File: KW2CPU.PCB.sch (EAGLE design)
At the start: 66 parts, among them J1 DF12_M, J2 MOLEX55560-0207, J3 MMCX_VERT, U1 MKW21D, U2 AT45DB161D8S1, U3 RF6555, U5 F-ANTENNA, X1 32KHZ, X2 32MHZ

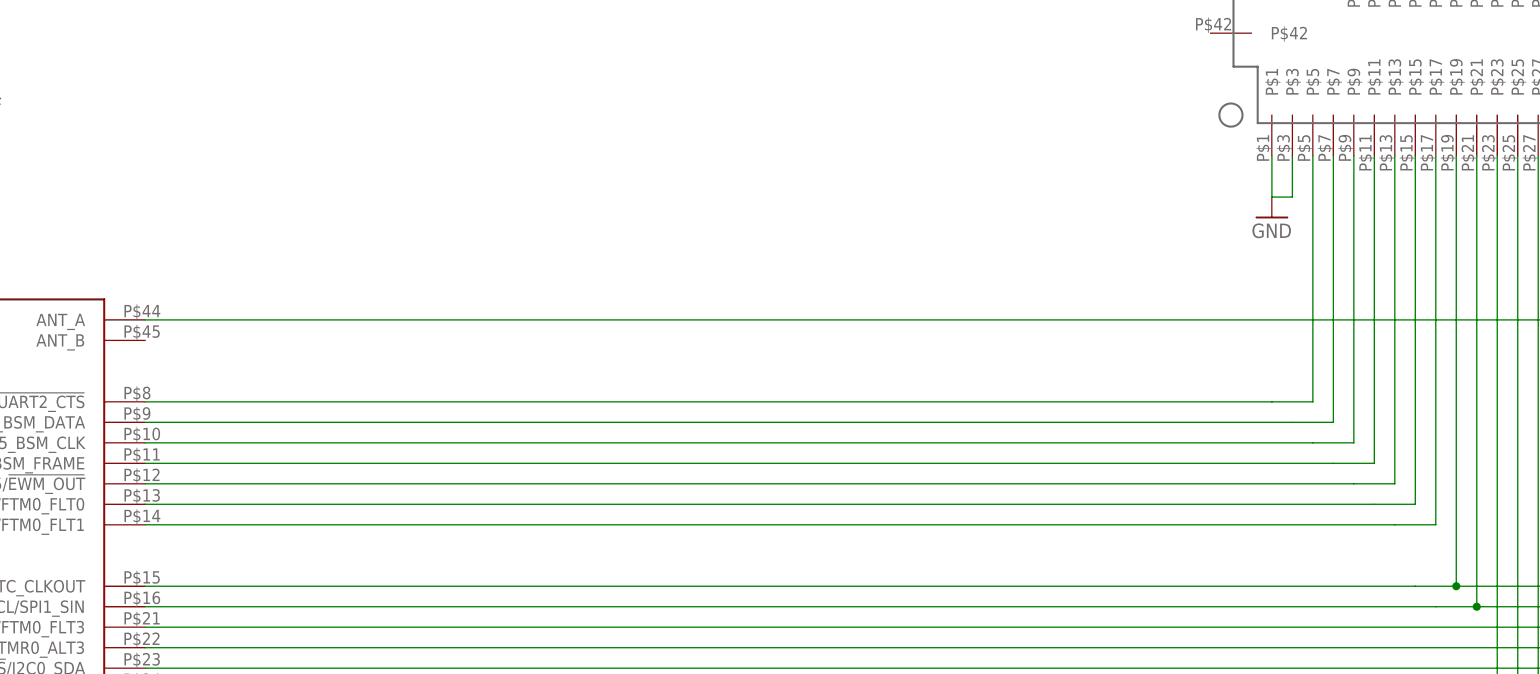
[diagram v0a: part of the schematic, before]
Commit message: Added timing TPs
For radio calibration. Also exported CAD model
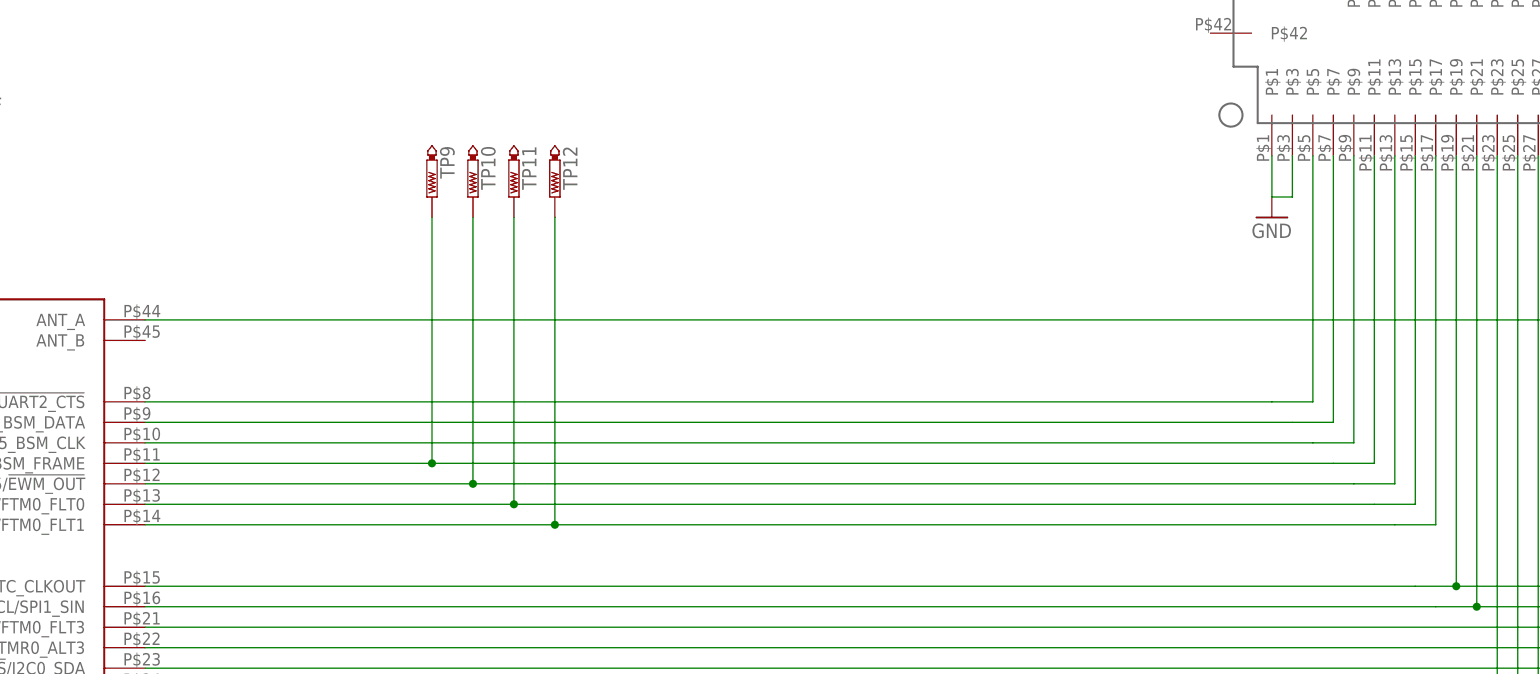
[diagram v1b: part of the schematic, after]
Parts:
- added TP10, TP11, TP12, TP9: PTR1TP15R, testpad:PTR1TP15R
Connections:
- net PTD4/LLWU_P14/MADC0_SE21/SPI0_PCS1/!UART0_RTS!/FTM0_CH4/EWM_IN/GPIO_BSM_FRAME: now also TP9.TP
- net PTD5/ADC0_SE6B/SPI0_PCS2/!UART0_CTS!/!UART0_COL!/FTM0_CH5/!EWM_OUT: now also TP10.TP
- net PTD6/LLWU_P15/ADC0_SE7B/SPI0_PCS3/UART0_RX/FTM0_CH6/FTM0_FLT0: now also TP11.TP
- net PTD7/MADC0_SE22/CMT_IRO/UART0_TX/FTM0_CH7/FTM0_FLT1: now also TP12.TP
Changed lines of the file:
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@@
 <part name="TP7" library="testpad" deviceset="PTR1" device="TP15R"/>
 <part name="TP8" library="testpad" deviceset="PTR1" device="TP15R"/>
+<part name="TP9" library="testpad" deviceset="PTR1" device="TP15R"/>
+<part name="TP10" library="testpad" deviceset="PTR1" device="TP15R"/>
+<part name="TP11" library="testpad" deviceset="PTR1" device="TP15R"/>
+<part name="TP12" library="testpad" deviceset="PTR1" device="TP15R"/>
 </parts>
 <sheets>
@@
 <instance part="TP7" gate="G$1" x="292.1" y="106.68" rot="R180"/>
 <instance part="TP8" gate="G$1" x="350.52" y="53.34" rot="R180"/>
+<instance part="TP9" gate="G$1" x="101.6" y="63.5" rot="R180"/>
+<instance part="TP10" gate="G$1" x="106.68" y="63.5" rot="R180"/>
+<instance part="TP11" gate="G$1" x="111.76" y="63.5" rot="R180"/>
+<instance part="TP12" gate="G$1" x="116.84" y="63.5" rot="R180"/>
 </instances>
 <busses>
@@
 <segment>
 <pinref part="U1" gate="G$1" pin="PTD4/LLWU_P14/MADC0_SE21/SPI0_PCS1/!UART0_RTS!/FTM0_CH4/EWM_IN/GPIO_BSM_FRAME"/>
-<wire x1="66.04" y1="30.48" x2="213.36" y2="30.48" width="0.1524" layer="91"/>
+<wire x1="66.04" y1="30.48" x2="101.6" y2="30.48" width="0.1524" layer="91"/>
 <pinref part="J1" gate="G$1" pin="P$11"/>
+<wire x1="101.6" y1="30.48" x2="213.36" y2="30.48" width="0.1524" layer="91"/>
 <wire x1="213.36" y1="30.48" x2="218.44" y2="30.48" width="0.1524" layer="91"/>
 <wire x1="218.44" y1="30.48" x2="218.44" y2="68.58" width="0.1524" layer="91"/>
+<pinref part="TP9" gate="G$1" pin="TP"/>
+<wire x1="101.6" y1="60.96" x2="101.6" y2="30.48" width="0.1524" layer="91"/>
+<junction x="101.6" y="30.48"/>
 </segment>
 </net>
@@
 <segment>
 <pinref part="U1" gate="G$1" pin="PTD5/ADC0_SE6B/SPI0_PCS2/!UART0_CTS!/!UART0_COL!/FTM0_CH5/!EWM_OUT"/>
-<wire x1="66.04" y1="27.94" x2="215.9" y2="27.94" width="0.1524" layer="91"/>
+<wire x1="66.04" y1="27.94" x2="106.68" y2="27.94" width="0.1524" layer="91"/>
 <pinref part="J1" gate="G$1" pin="P$13"/>
+<wire x1="106.68" y1="27.94" x2="215.9" y2="27.94" width="0.1524" layer="91"/>
 <wire x1="215.9" y1="27.94" x2="220.98" y2="27.94" width="0.1524" layer="91"/>
 <wire x1="220.98" y1="27.94" x2="220.98" y2="68.58" width="0.1524" layer="91"/>
+<pinref part="TP10" gate="G$1" pin="TP"/>
+<wire x1="106.68" y1="60.96" x2="106.68" y2="27.94" width="0.1524" layer="91"/>
+<junction x="106.68" y="27.94"/>
 </segment>
 </net>
@@
 <segment>
 <pinref part="U1" gate="G$1" pin="PTD6/LLWU_P15/ADC0_SE7B/SPI0_PCS3/UART0_RX/FTM0_CH6/FTM0_FLT0"/>
-<wire x1="66.04" y1="25.4" x2="218.44" y2="25.4" width="0.1524" layer="91"/>
+<wire x1="66.04" y1="25.4" x2="111.76" y2="25.4" width="0.1524" layer="91"/>
 <pinref part="J1" gate="G$1" pin="P$15"/>
+<wire x1="111.76" y1="25.4" x2="218.44" y2="25.4" width="0.1524" layer="91"/>
 <wire x1="218.44" y1="25.4" x2="223.52" y2="25.4" width="0.1524" layer="91"/>
 <wire x1="223.52" y1="25.4" x2="223.52" y2="68.58" width="0.1524" layer="91"/>
+<pinref part="TP11" gate="G$1" pin="TP"/>
+<wire x1="111.76" y1="60.96" x2="111.76" y2="25.4" width="0.1524" layer="91"/>
+<junction x="111.76" y="25.4"/>
 </segment>
 </net>
@@
 <segment>
 <pinref part="U1" gate="G$1" pin="PTD7/MADC0_SE22/CMT_IRO/UART0_TX/FTM0_CH7/FTM0_FLT1"/>
-<wire x1="66.04" y1="22.86" x2="220.98" y2="22.86" width="0.1524" layer="91"/>
+<wire x1="66.04" y1="22.86" x2="116.84" y2="22.86" width="0.1524" layer="91"/>
 <pinref part="J1" gate="G$1" pin="P$17"/>
+<wire x1="116.84" y1="22.86" x2="220.98" y2="22.86" width="0.1524" layer="91"/>
 <wire x1="220.98" y1="22.86" x2="226.06" y2="22.86" width="0.1524" layer="91"/>
 <wire x1="226.06" y1="22.86" x2="226.06" y2="68.58" width="0.1524" layer="91"/>
-</segment>
-</net>
+<pinref part="TP12" gate="G$1" pin="TP"/>
+<wire x1="116.84" y1="60.96" x2="116.84" y2="22.86" width="0.1524" layer="91"/>
+<junction x="116.84" y="22.86"/>
+</segment>
+</net>

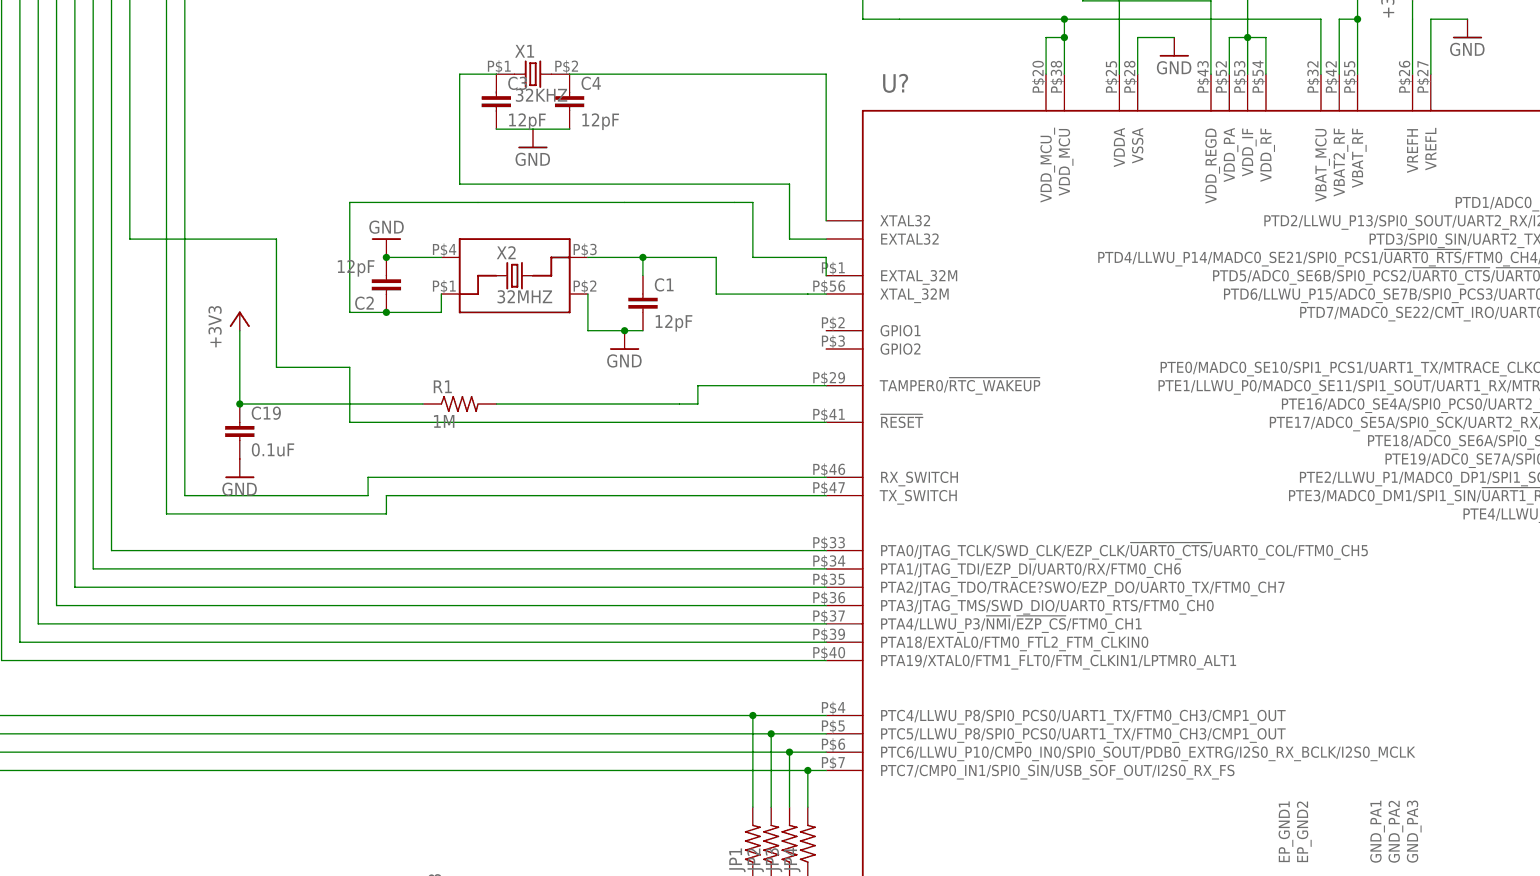
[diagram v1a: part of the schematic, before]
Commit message: Fixed PTC5 label and added RESET pullup
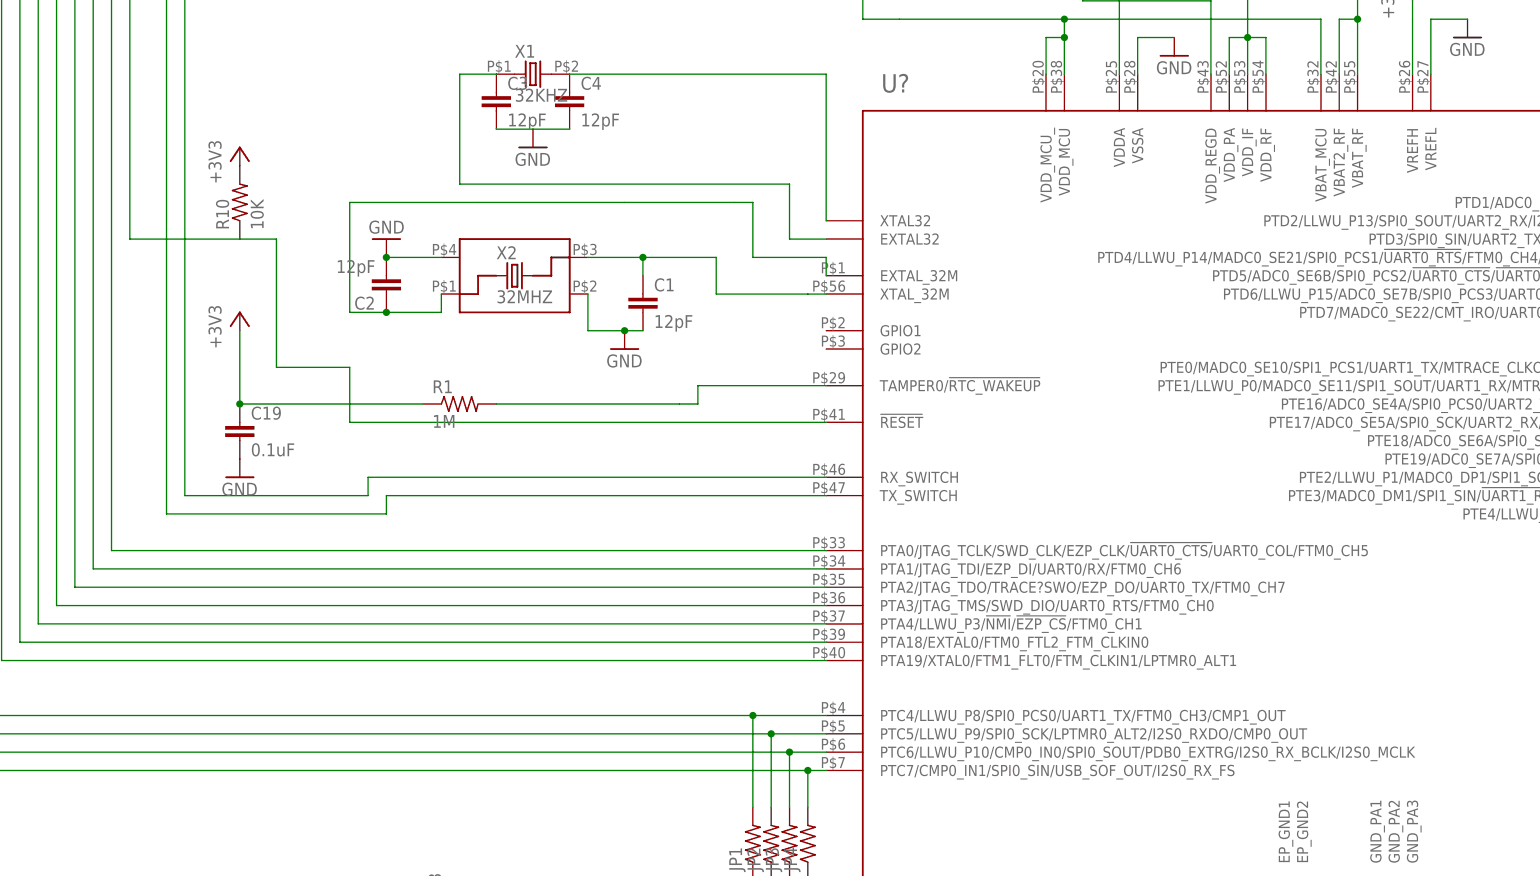
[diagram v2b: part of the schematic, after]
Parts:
- added R10: 10K, GW-devices:RF-R0402
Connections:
- net !RESET: now also R10.1
- net +3V3: now also R10.2
- net PTC5/LLWU_P8/SPI0_PCS0/UART1_TX/FTM0_CH3/CMP1_OUT: now also U1.PTC5/LLWU_P9/SPI0_SCK/LPTMR0_ALT2/I2S0_RXDO/CMP0_OUT; no longer U1.PTC5/LLWU_P8/SPI0_PCS0/UART1_TX/FTM0_CH3/CMP1_OUT
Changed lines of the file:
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@@
 <part name="TP11" library="testpad" deviceset="PTR1" device="TP15R"/>
 <part name="TP12" library="testpad" deviceset="PTR1" device="TP15R"/>
+<part name="R10" library="GW-devices" deviceset="RF-R" device="0402" value="10K"/>
+<part name="+3V14" library="supply1" deviceset="+3V3" device=""/>
 </parts>
 <sheets>
@@
 <instance part="TP11" gate="G$1" x="111.76" y="63.5" rot="R180"/>
 <instance part="TP12" gate="G$1" x="116.84" y="63.5" rot="R180"/>
+<instance part="R10" gate="G$1" x="-147.32" y="38.1" rot="R90"/>
+<instance part="+3V14" gate="G$1" x="-147.32" y="45.72"/>
 </instances>
 <busses>
@@
 <pinref part="J2" gate="G$1" pin="P$1"/>
 </segment>
+<segment>
+<pinref part="R10" gate="G$1" pin="2"/>
+<pinref part="+3V14" gate="G$1" pin="+3V3"/>
+</segment>
 </net>
 <net name="EXTAL_32M" class="0">
@@
 <net name="PTC5/LLWU_P8/SPI0_PCS0/UART1_TX/FTM0_CH3/CMP1_OUT" class="0">
 <segment>
-<pinref part="U1" gate="G$1" pin="PTC5/LLWU_P8/SPI0_PCS0/UART1_TX/FTM0_CH3/CMP1_OUT"/>
+<pinref part="U1" gate="G$1" pin="PTC5/LLWU_P9/SPI0_SCK/LPTMR0_ALT2/I2S0_RXDO/CMP0_OUT"/>
 <wire x1="-73.66" y1="-35.56" x2="-66.04" y2="-35.56" width="0.1524" layer="91"/>
 <pinref part="J1" gate="G$1" pin="P$24"/>
@@
 <wire x1="-132.08" y1="15.24" x2="-142.24" y2="15.24" width="0.1524" layer="91"/>
 <wire x1="-142.24" y1="15.24" x2="-142.24" y2="33.02" width="0.1524" layer="91"/>
-<wire x1="-142.24" y1="33.02" x2="-162.56" y2="33.02" width="0.1524" layer="91"/>
+<wire x1="-142.24" y1="33.02" x2="-147.32" y2="33.02" width="0.1524" layer="91"/>
+<wire x1="-147.32" y1="33.02" x2="-162.56" y2="33.02" width="0.1524" layer="91"/>
 <wire x1="-162.56" y1="33.02" x2="-162.56" y2="121.92" width="0.1524" layer="91"/>
 <wire x1="-162.56" y1="121.92" x2="205.74" y2="121.92" width="0.1524" layer="91"/>
@@
 <wire x1="297.18" y1="142.24" x2="297.18" y2="121.92" width="0.1524" layer="91"/>
 <junction x="297.18" y="121.92"/>
-</segment>
-</net>
+<pinref part="R10" gate="G$1" pin="1"/>
+</segment>
+</net>

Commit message: Switched Flash for EEPROM
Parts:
- removed JP1, JP2, JP3, JP4: (no value), GW-devices:RF-R0402
- removed R2, R3: 10k, GW-devices:RF-R0402
- removed U2: AT45DB161D8S1, KW2:AT45DB161D8S1
- added IC1: 25AA080SN, microchip:25AA080SN
- added R11, R12: 10k, GW-devices:RF-R0402
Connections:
- removed net !CS: JP1.1, U2.!CS
- removed net N$54: JP4.1, U2.SO
- removed net N$8: R3.1, U2.!RESET
- removed net N$9: R2.1, U2.!WP
- removed net SCK: JP2.1, U2.SCK
- removed net SI: JP3.1, U2.SI
- new net N$1: IC1.!WP, R11.1
- new net N$2: IC1.!HOLD, R12.1
- net +3V3: now also IC1.VCC, R11.2, R12.2; no longer R2.2, R3.2, U2.VCC
- net GND: now also IC1.GND; no longer U2.GND
- net PTC4/LLWU_P8/SPI0_PCS0/UART1_TX/FTM0_CH3/CMP1_OUT: no longer JP1.2
- net PTC5/LLWU_P8/SPI0_PCS0/UART1_TX/FTM0_CH3/CMP1_OUT: now also IC1.SCK; no longer JP2.2
- net PTC6/LLWU_P10/CMP0_IN0/SPI0_SOUT/PDB0_EXTRG/I2S0_RX_BCLK/I2S0_MCLK: now also IC1.SI; no longer JP3.2
- net PTC7/CMP0_IN1/SPI0_SIN/USB_SOF_OUT/I2S0_RX_FS: now also IC1.SO; no longer JP4.2
- net PTD5/ADC0_SE6B/SPI0_PCS2/!UART0_CTS!/!UART0_COL!/FTM0_CH5/!EWM_OUT: now also IC1.!CS
